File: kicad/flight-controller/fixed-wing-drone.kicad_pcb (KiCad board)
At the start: 4 copper layers, 91 x 61.5 mm, 78 parts, among them J1 1, J10 UWB SPI, J11 Inter ESP UART, J13 USB-C, J14 GPS/Compass, J15 Airspeed I2C, J16 8, J19 ESC2, J2 2, J20 FC UBEC Input, J22 ESC1, J3 3, J4 4, J5 5, J6 6, J7 RC Conn, J8 LIDAR I2C, J9 7, M2 MountingHole_2.2mm_M2, Q1 reverse polarity protection, Q2 reverse polarity protection, SW1 TS-1088, SW2 TS-1088, U1 ESP32-S3-WROOM-1, U2 Primary IMU, U3 Backup IMU, U5 AP2112K-3.3, U6 AP2112K-3.3, U7 Barometer

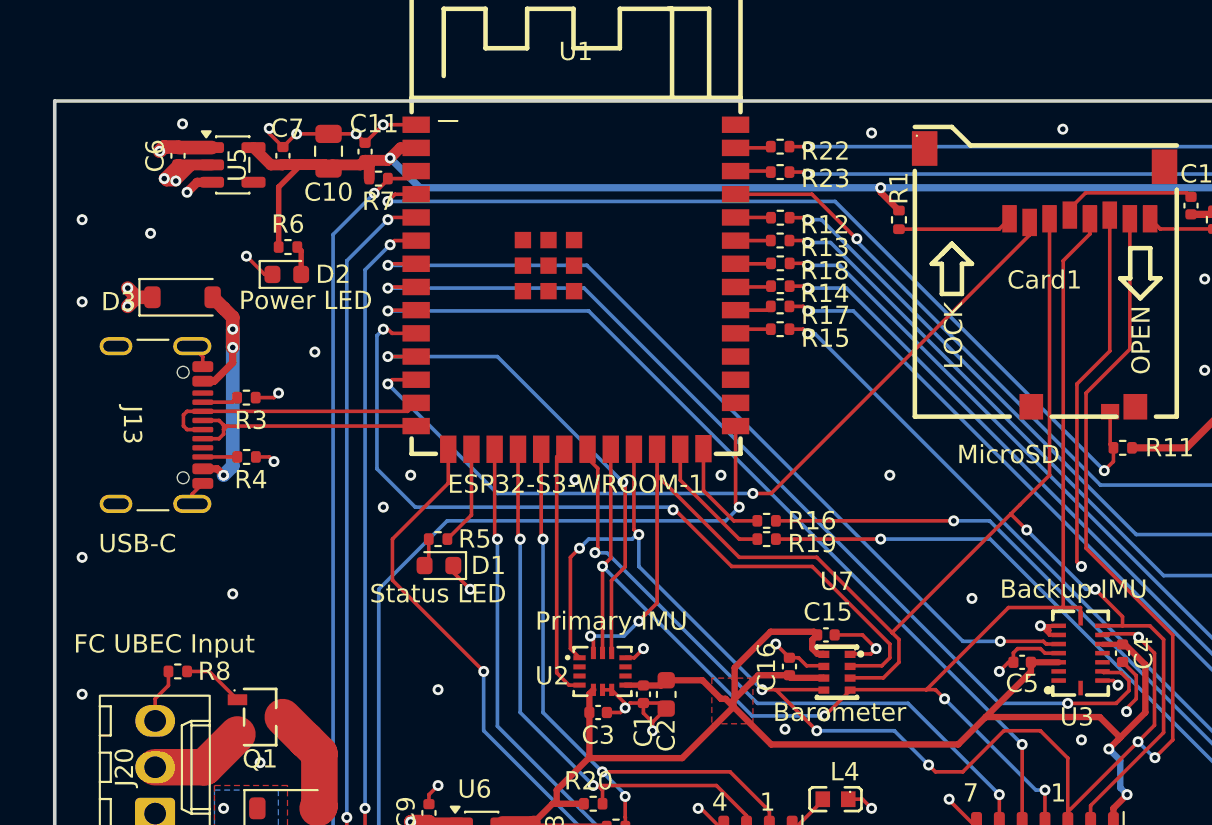
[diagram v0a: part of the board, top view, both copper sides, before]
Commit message: Fix ESP32 LDO thermal margin, add USB-C/SBUS ESD protection
Design review flagged the ESP32-S3's 3.3V LDO (AP2112K-3.3, SOT-23-5)
at only 1.5C margin to absolute max under WiFi load. Swapped to a
Torex XC6220B331PR-G (SOT-89-5, thermal tab tied to GND) with matching
input/output caps and thermal vias under the tab; thermal score is now
100/100 with no findings. Sensor LDO (U6) was unaffected and left as-is.

Also added TVS protection that was missing on two exposed signal paths:
D4 + bulk cap on USB-C VBUS (J13, now populated for field use) ahead of
the existing blocking diode, and a matching TVS (D6) on the RC receiver
SBUS line (J7), reusing the same part to minimize BOM diversity.

Every part number touched this pass (U4, C17-C19, D4, D6) was verified
against real distributor data, and a full BOM audit confirmed all other
assigned part numbers match their stated value and footprint. Also
removed two orphaned, unwired schematic files (airspeed.kicad_sch,
lidar.kicad_sch) that weren't in the sheet hierarchy.

Known follow-up before fab: the production/ fab package predates this
rework and needs to be regenerated, and Update PCB from Schematic needs
a re-run to sync D4/D6's display value (nets are already correct).

Co-Authored-By: Claude Sonnet 5 <noreply@anthropic.com>
Claude-Session: https://claude.ai/code/session_01NksRnW4jXLWsYwZNR7u39H
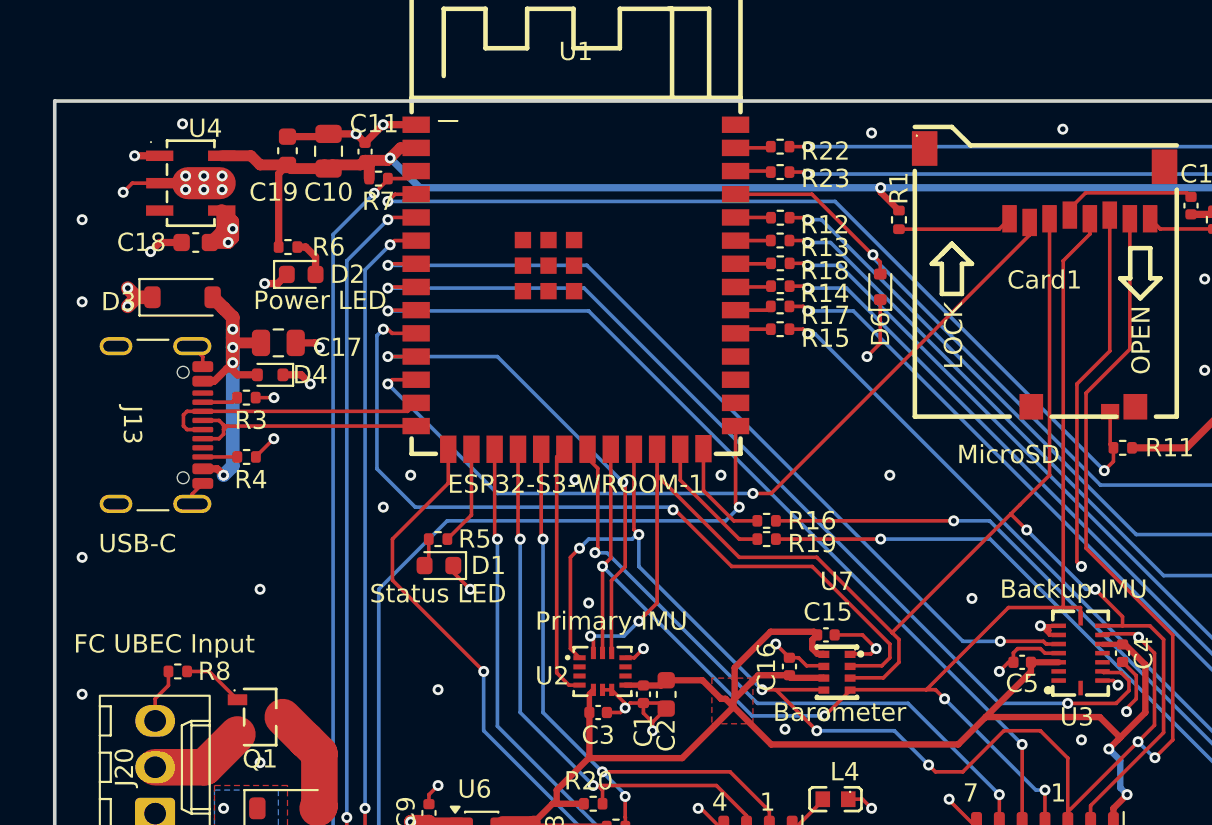
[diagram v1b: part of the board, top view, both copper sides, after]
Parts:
- removed C6, C7: 1uF, Capacitor_SMD:C_0402_1005Metric
- removed U5: AP2112K-3.3, Package_TO_SOT_SMD:SOT-23-5
- added C17: 10uF, Capacitor_SMD:C_0805_2012Metric, F.Cu at (110.5, 75.5)
- added C18: 10uF, Capacitor_SMD:C_0603_1608Metric, F.Cu at (106.0, 70.0)
- added C19: 4.7uF, Capacitor_SMD:C_0603_1608Metric, F.Cu at (111.0, 65.0)
- added D4: ESD5Z5.0T1G, Diode_SMD:D_SOD-523, F.Cu at (110.0, 77.2)
- added D6: ESD5Z5.0T1G, Diode_SMD:D_SOD-523, F.Cu at (143.5, 72.4)
- added U4: XC6220B331PR-G, easyeda2kicad:SOT-89-5_L4.5-W2.5-P1.50-LS4.4-BR, F.Cu at (105.7, 66.8)
- moved D2 0.79 mm to (111.8, 71.8)
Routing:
- net GND: track 96.1 -> 102.2 mm, vias 93 -> 99
- net Net-(D3-A): track 15.6 -> 19.1 mm, vias 3 -> 4
- net /FC_5V: track 15.8 -> 18.5 mm, vias 13 -> 14
- net /ESP_3V3: track 84.7 -> 86.2 mm
- net /RC_SBUS: track 44.3 -> 45.5 mm
- net Net-(D2-A): track 1.59 -> 2.19 mm
